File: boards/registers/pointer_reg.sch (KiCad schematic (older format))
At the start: 80 parts, among them U10 74ACT161, U11 74ACT244, U12 74ACT244, U13 74ACT161, U14 74ACT161, U15 74ACT244, U16 74ACT244, U9 74ACT161

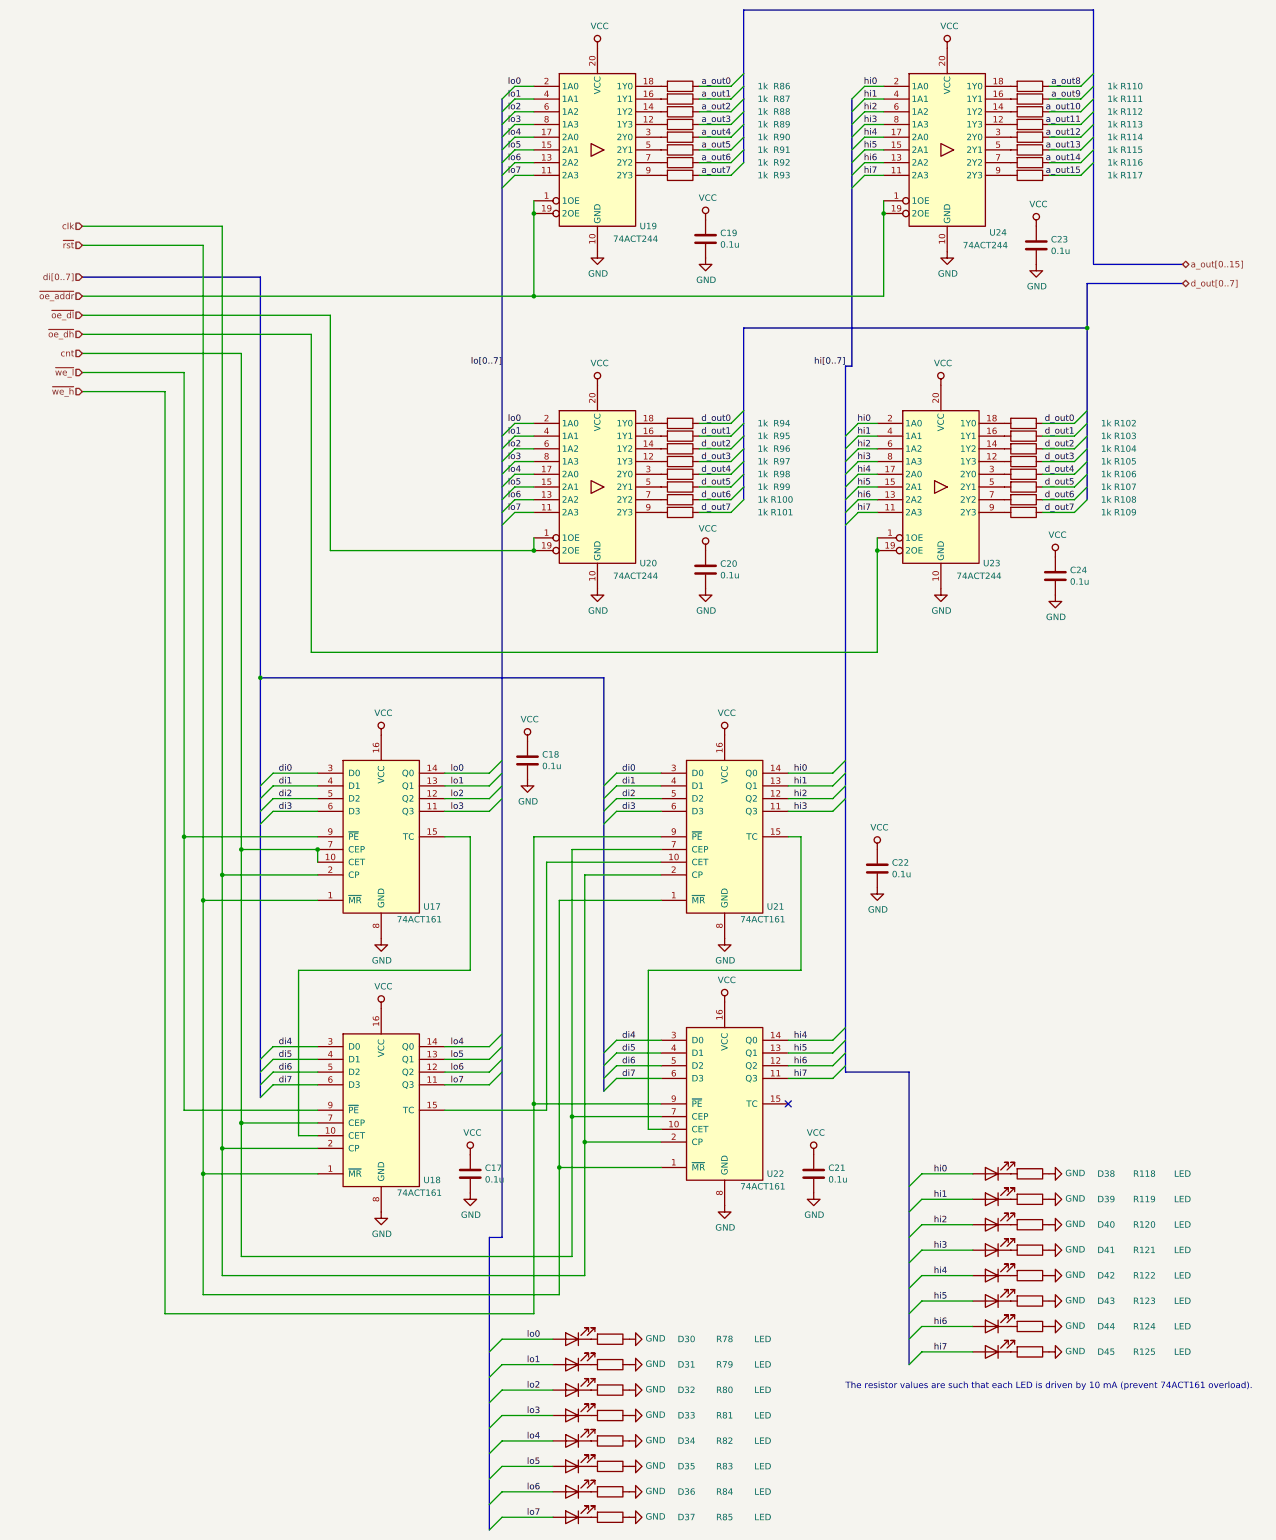
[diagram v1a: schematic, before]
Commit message: CPU registers board
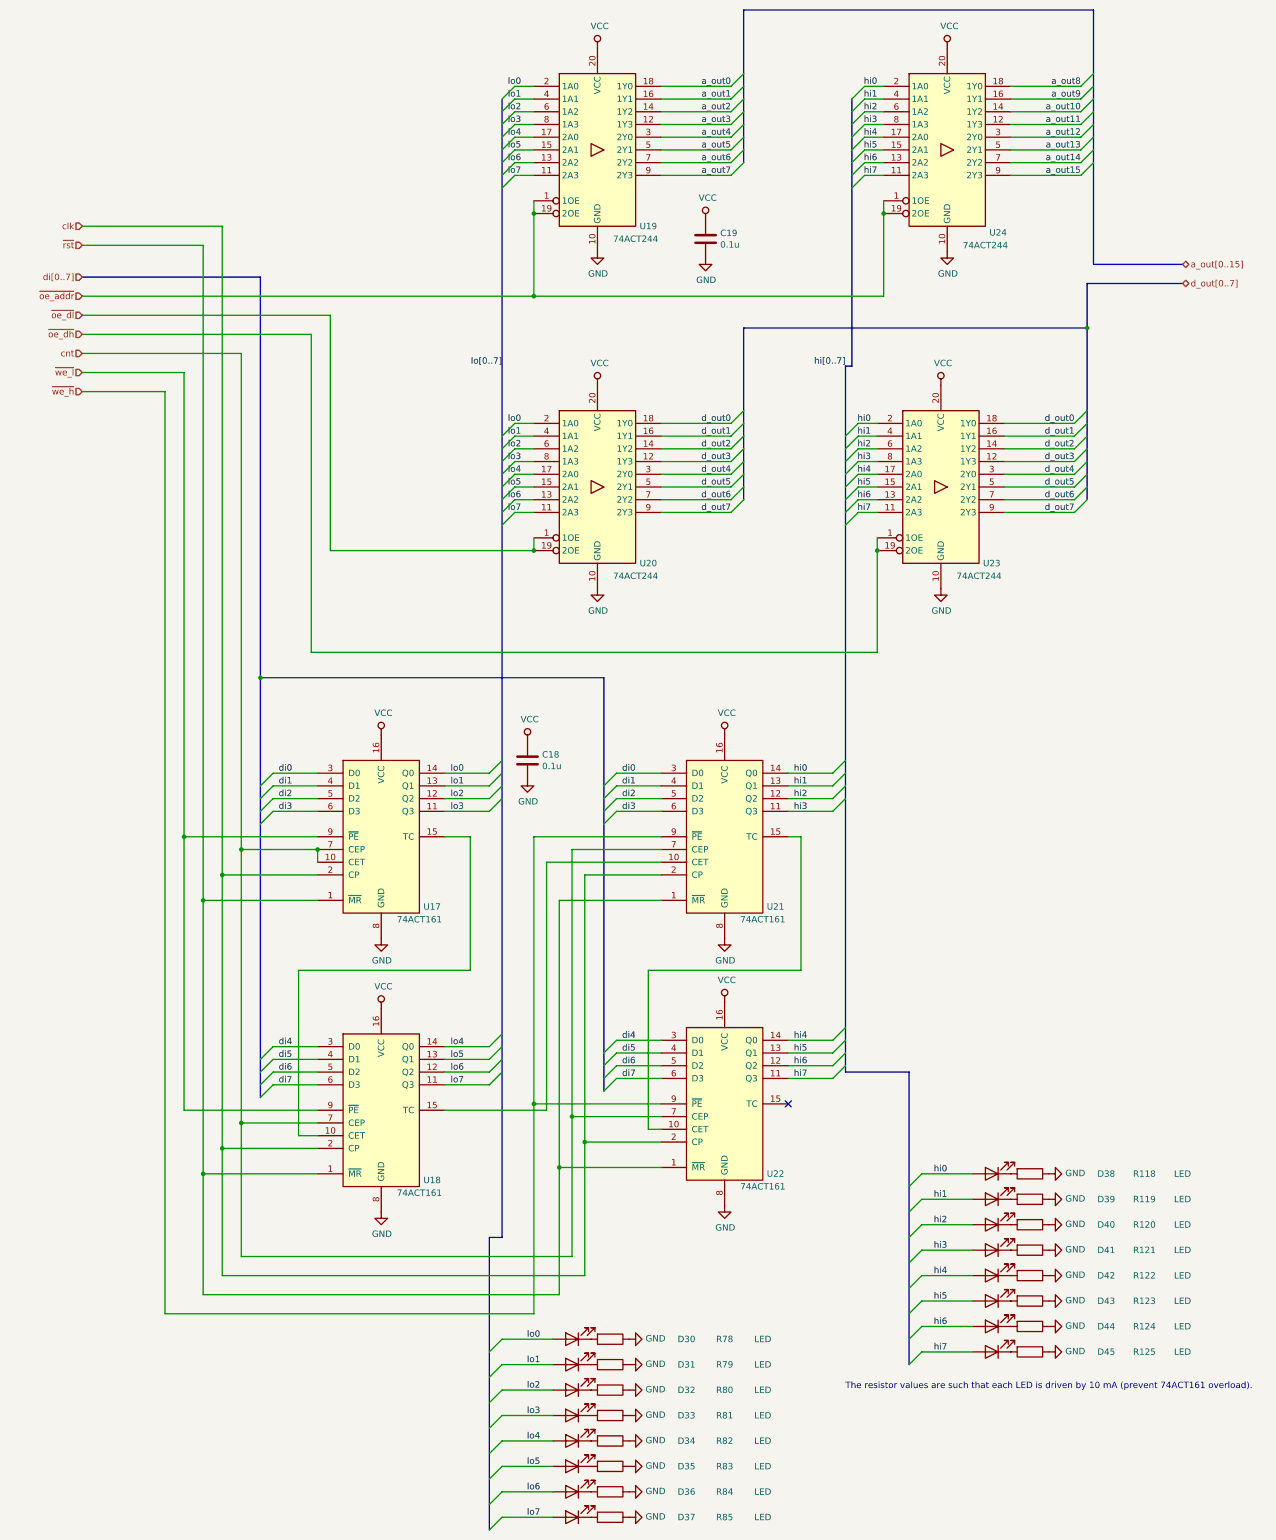
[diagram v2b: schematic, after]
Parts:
- removed C12, C13, C14, C15, C16, C9: 0.1u, Capacitor_SMD:C_0805_2012Metric, symbol Device:C
- removed R38, R39, R40, R41, R42, R43, R44, R45, R46, R47, R48, R49, R50, R51, R52, R53, R54, R55, R56, R57, R58, R59, R60, R61, R62, R63, R64, R65, R66, R67, R68, R69: 1k, Resistor_SMD:R_0805_2012Metric, symbol Device:R
- U11, U12, U15, U16: footprint Package_SO:SO-20_12.8x7.5mm_P1.27mm -> Package_SO:TSSOP-20_4.4x6.5mm_P0.65mm
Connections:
- net a_out0: now also U11.18 (1Y0)
- net a_out1: now also U11.16 (1Y1)
- net a_out10: now also U16.14 (1Y2)
- net a_out11: now also U16.12 (1Y3)
- net a_out12: now also U16.3 (2Y0)
- net a_out13: now also U16.5 (2Y1)
- net a_out14: now also U16.7 (2Y2)
- net a_out15: now also U16.9 (2Y3)
- net a_out2: now also U11.14 (1Y2)
- net a_out3: now also U11.12 (1Y3)
- net a_out4: now also U11.3 (2Y0)
- net a_out5: now also U11.5 (2Y1)
- net a_out6: now also U11.7 (2Y2)
- net a_out7: now also U11.9 (2Y3)
- net a_out8: now also U16.18 (1Y0)
- net a_out9: now also U16.16 (1Y1)
- net d_out0: now also U12.18 (1Y0), U15.18 (1Y0)
- net d_out1: now also U12.16 (1Y1), U15.16 (1Y1)
- net d_out2: now also U12.14 (1Y2), U15.14 (1Y2)
- net d_out3: now also U12.12 (1Y3), U15.12 (1Y3)
- net d_out4: now also U12.3 (2Y0), U15.3 (2Y0)
- net d_out5: now also U12.5 (2Y1), U15.5 (2Y1)
- net d_out6: now also U12.7 (2Y2), U15.7 (2Y2)
- net d_out7: now also U12.9 (2Y3), U15.9 (2Y3)

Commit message: Fixed some footprints
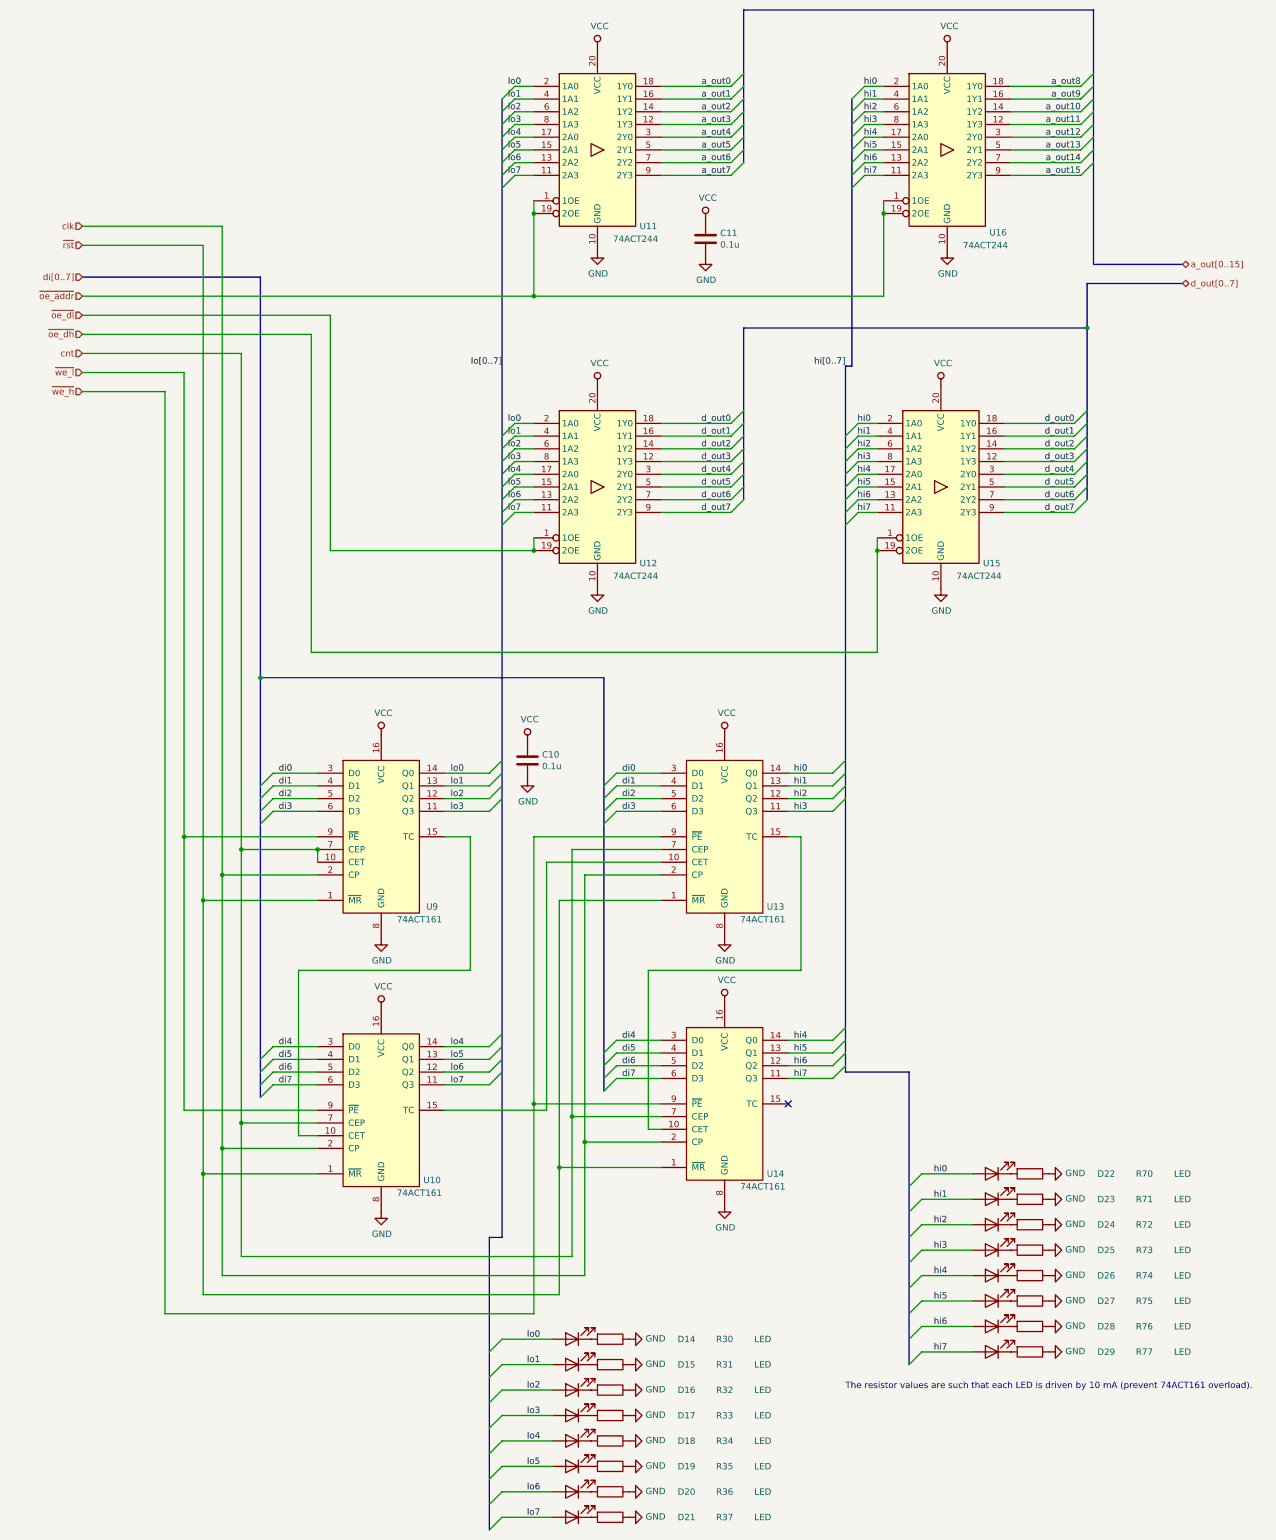
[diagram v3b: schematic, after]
